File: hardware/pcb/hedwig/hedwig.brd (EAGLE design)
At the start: 60 x 60 mm, 85 parts, among them J1 DX07B024JJ1R1500, P1 JTAG-10MINI, P2 SENSOR_SCL, P3 RF_SCK, P4 PC1, P5 PC5, P6 PC9, Q1 16MHz, Q2 IRLML6402, Q3 20V/0.2A/8MHz/1.2Ω/1Vth, Q6 20V/0.2A/8MHz/1.2Ω/1Vth, U1 NRF24L01SMD, U2 TEXAS_INSTRUMENTS_TLC59731DRT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, U3 FT232RQ, U4 TPS7A26-1.8, U5 ADP2302, U6 9DoF IMU, U7 MPL3115A2LGA, X1 8M, X2 32.768

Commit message: Added pics, pdf, fixed silkscreen, and added more vias
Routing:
- net GND: vias 67 -> 99
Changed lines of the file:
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@@
 <layer number="25" name="tNames" color="7" fill="1" visible="yes" active="yes"/>
 <layer number="26" name="bNames" color="7" fill="1" visible="yes" active="yes"/>
-<layer number="27" name="tValues" color="7" fill="1" visible="no" active="yes"/>
-<layer number="28" name="bValues" color="7" fill="1" visible="no" active="yes"/>
+<layer number="27" name="tValues" color="7" fill="1" visible="yes" active="yes"/>
+<layer number="28" name="bValues" color="7" fill="1" visible="yes" active="yes"/>
 <layer number="29" name="tStop" color="7" fill="3" visible="yes" active="yes"/>
 <layer number="30" name="bStop" color="7" fill="6" visible="yes" active="yes"/>
@@
 <layer number="39" name="tKeepout" color="4" fill="11" visible="yes" active="yes"/>
 <layer number="40" name="bKeepout" color="1" fill="11" visible="yes" active="yes"/>
-<layer number="41" name="tRestrict" color="4" fill="10" visible="yes" active="yes"/>
-<layer number="42" name="bRestrict" color="1" fill="10" visible="yes" active="yes"/>
-<layer number="43" name="vRestrict" color="2" fill="10" visible="yes" active="yes"/>
-<layer number="44" name="Drills" color="7" fill="1" visible="yes" active="yes"/>
-<layer number="45" name="Holes" color="7" fill="1" visible="yes" active="yes"/>
-<layer number="46" name="Milling" color="3" fill="1" visible="yes" active="yes"/>
-<layer number="47" name="Measures" color="7" fill="1" visible="yes" active="yes"/>
-<layer number="48" name="Document" color="7" fill="1" visible="yes" active="yes"/>
-<layer number="49" name="Reference" color="7" fill="1" visible="yes" active="yes"/>
+<layer number="41" name="tRestrict" color="4" fill="10" visible="no" active="yes"/>
+<layer number="42" name="bRestrict" color="1" fill="10" visible="no" active="yes"/>
+<layer number="43" name="vRestrict" color="2" fill="10" visible="no" active="yes"/>
+<layer number="44" name="Drills" color="7" fill="1" visible="no" active="yes"/>
+<layer number="45" name="Holes" color="7" fill="1" visible="no" active="yes"/>
+<layer number="46" name="Milling" color="3" fill="1" visible="no" active="yes"/>
+<layer number="47" name="Measures" color="7" fill="1" visible="no" active="yes"/>
+<layer number="48" name="Document" color="7" fill="1" visible="no" active="yes"/>
+<layer number="49" name="Reference" color="7" fill="1" visible="no" active="yes"/>
 <layer number="50" name="dxf" color="7" fill="1" visible="no" active="no"/>
-<layer number="51" name="tDocu" color="7" fill="1" visible="yes" active="yes"/>
-<layer number="52" name="bDocu" color="7" fill="1" visible="yes" active="yes"/>
+<layer number="51" name="tDocu" color="7" fill="1" visible="no" active="yes"/>
+<layer number="52" name="bDocu" color="7" fill="1" visible="no" active="yes"/>
 <layer number="53" name="tGND_GNDA" color="7" fill="9" visible="no" active="no"/>
 <layer number="54" name="bGND_GNDA" color="1" fill="9" visible="no" active="no"/>
@@
 <layer number="99" name="SpiceOrder" color="7" fill="1" visible="no" active="no"/>
 <layer number="100" name="Muster" color="7" fill="1" visible="no" active="no"/>
-<layer number="101" name="Patch_Top" color="12" fill="4" visible="yes" active="yes"/>
+<layer number="101" name="Patch_Top" color="12" fill="4" visible="no" active="yes"/>
 <layer number="102" name="Vscore" color="7" fill="1" visible="no" active="yes"/>
 <layer number="103" name="tMap" color="7" fill="1" visible="no" active="yes"/>
@@
 <layer number="131" name="tAdjust" color="7" fill="1" visible="no" active="no"/>
 <layer number="132" name="bAdjust" color="7" fill="1" visible="no" active="no"/>
-<layer number="144" name="Drill_legend" color="7" fill="1" visible="yes" active="yes"/>
+<layer number="144" name="Drill_legend" color="7" fill="1" visible="no" active="yes"/>
 <layer number="150" name="Notes" color="7" fill="1" visible="no" active="no"/>
 <layer number="151" name="HeatSink" color="7" fill="1" visible="no" active="yes"/>
@@
 <layer number="155" name="FabDoc3" color="7" fill="1" visible="no" active="no"/>
 <layer number="199" name="Contour" color="7" fill="1" visible="no" active="no"/>
-<layer number="200" name="200bmp" color="1" fill="10" visible="yes" active="yes"/>
+<layer number="200" name="200bmp" color="1" fill="10" visible="no" active="yes"/>
 <layer number="201" name="201bmp" color="2" fill="10" visible="no" active="yes"/>
 <layer number="202" name="202bmp" color="3" fill="1" visible="no" active="no"/>
@@
 <text x="5.156140625" y="4.1582" size="0.3048" layer="22" rot="MR0">RF_MOSI</text>
 <text x="5.1028" y="0.1983375" size="0.3048" layer="22" rot="MR0">PC1</text>
-<text x="-137.5003625" y="10.09776875" size="0.3048" layer="22" rot="MR270">PC3</text>
+<text x="5.27176875" y="-3.8506375" size="0.3048" layer="22" rot="MR0">PC3</text>
 <text x="5.30091875" y="-7.8839375" size="0.3048" layer="22" rot="MR0">PC5</text>
 <text x="5.2425" y="-11.87046875" size="0.3048" layer="22" rot="MR0">PC7</text>
@@
 <rectangle x1="-16.8148" y1="1.27" x2="-16.7132" y2="1.3716" layer="22" rot="R90"/>
 <rectangle x1="-16.9164" y1="1.27" x2="-16.8148" y2="1.3716" layer="22" rot="R90"/>
-<text x="28.0416" y="-3.556" size="0.381" layer="22" font="vector" rot="R90">Designed by Adam in California
+<text x="27.9146" y="4.445" size="0.381" layer="22" font="vector" rot="MR270">Designed by Adam in California
       (while Devin watched)</text>
 </plain>
@@
 <via x="11.43" y="27.94" extent="1-16" drill="0.35"/>
 <via x="20.32" y="21.59" extent="1-16" drill="0.35"/>
+<via x="21.59" y="-3.81" extent="1-16" drill="0.35"/>
+<via x="26.67" y="17.78" extent="1-16" drill="0.35"/>
+<via x="24.13" y="17.78" extent="1-16" drill="0.35"/>
+<via x="19.05" y="19.05" extent="1-16" drill="0.35"/>
+<via x="20.32" y="15.24" extent="1-16" drill="0.35"/>
+<via x="26.67" y="13.97" extent="1-16" drill="0.35"/>
+<via x="25.4" y="8.89" extent="1-16" drill="0.35"/>
+<via x="13.97" y="20.32" extent="1-16" drill="0.35"/>
+<via x="25.4" y="15.24" extent="1-16" drill="0.35"/>
+<via x="25.4" y="19.05" extent="1-16" drill="0.35"/>
+<via x="12.7" y="-2.54" extent="1-16" drill="0.35"/>
+<via x="2.54" y="-12.7" extent="1-16" drill="0.35"/>
+<via x="-6.35" y="-26.67" extent="1-16" drill="0.35"/>
+<via x="2.54" y="-25.4" extent="1-16" drill="0.35"/>
+<via x="15.494" y="-10.16" extent="1-16" drill="0.35"/>
+<via x="26.416" y="-12.7" extent="1-16" drill="0.35"/>
+<via x="16.129" y="-4.191" extent="1-16" drill="0.35"/>
+<via x="25.527" y="-3.048" extent="1-16" drill="0.35"/>
+<via x="12.573" y="-13.081" extent="1-16" drill="0.35"/>
+<via x="20.574" y="-12.954" extent="1-16" drill="0.35"/>
+<via x="18.923" y="-22.352" extent="1-16" drill="0.35"/>
+<via x="9.779" y="-20.066" extent="1-16" drill="0.35"/>
+<via x="5.461" y="-17.018" extent="1-16" drill="0.35"/>
+<via x="6.731" y="-9.779" extent="1-16" drill="0.35"/>
+<via x="4.064" y="6.477" extent="1-16" drill="0.35"/>
+<via x="2.286" y="5.334" extent="1-16" drill="0.35"/>
+<via x="26.162" y="2.921" extent="1-16" drill="0.35"/>
+<via x="20.32" y="2.921" extent="1-16" drill="0.35"/>
+<via x="-22.86" y="-5.715" extent="1-16" drill="0.35"/>
+<via x="-19.05" y="-6.477" extent="1-16" drill="0.35"/>
+<via x="-26.289" y="-4.064" extent="1-16" drill="0.35"/>
+<via x="-25.781" y="-15.113" extent="1-16" drill="0.35"/>
 </signal>
 <signal name="NRST">

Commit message: Fix major issues in hardware
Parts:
- C10, C11, C8, C9: value 0.1uF -> 8.2pF
- C14: value 0.1uF -> 2.2uF
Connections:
- removed net B_VBUS: J1.B4, J1.B9
- removed net N$25: 5V_BAT.1, Q2.P3
- new net N$34: 5V_BAT.1, Q2.P2
- net +3V3: now also U$1.13
- net +5V: no longer Q2.P2
- net GND: now also U$1.12
- net USB_VCC: now also J1.B4, J1.B9
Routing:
- net N$25: track 35.3 -> 0.00 mm
- net +3V3: track 408.2 -> 416.8 mm
- net B_VBUS: track 6.42 -> 0.00 mm, vias 2 -> 0
- net +5V: track 30.5 -> 27.4 mm
- net USB_VCC: track 41.5 -> 42.5 mm

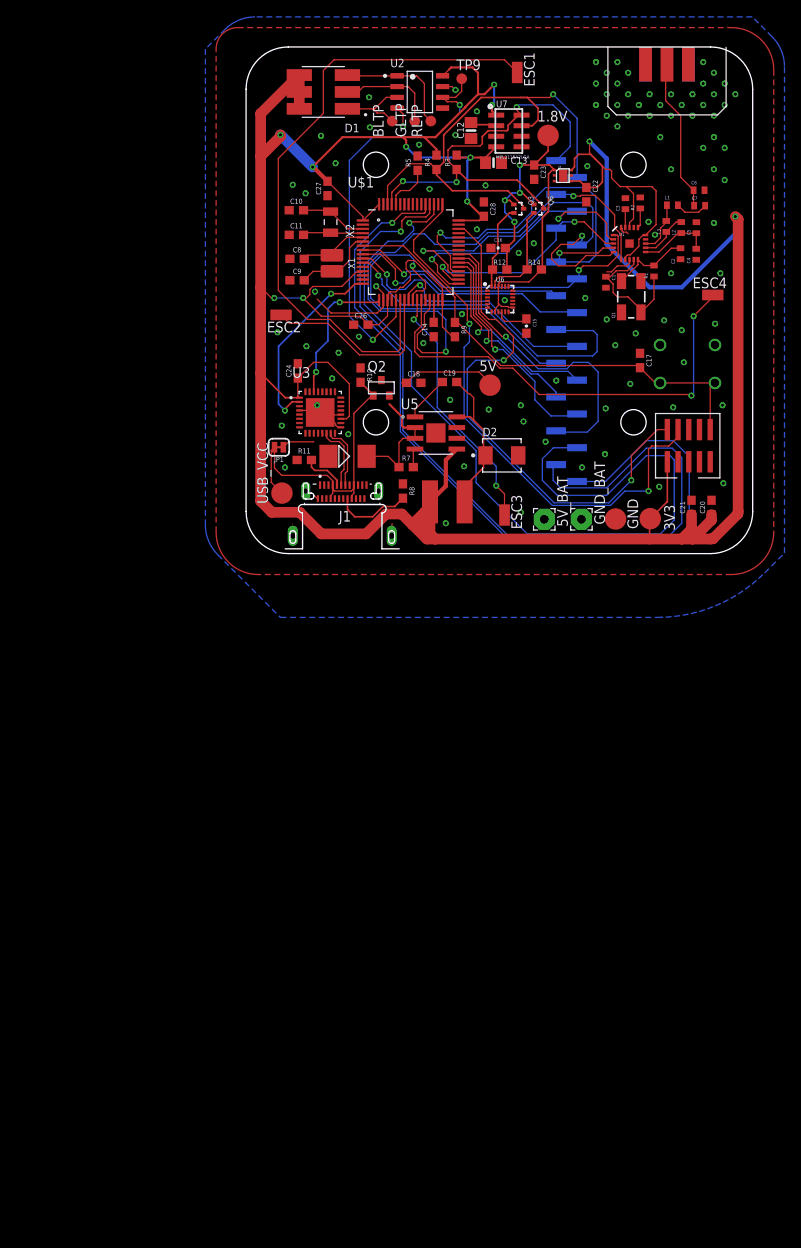
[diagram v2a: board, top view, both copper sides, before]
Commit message: schematic and pcb update
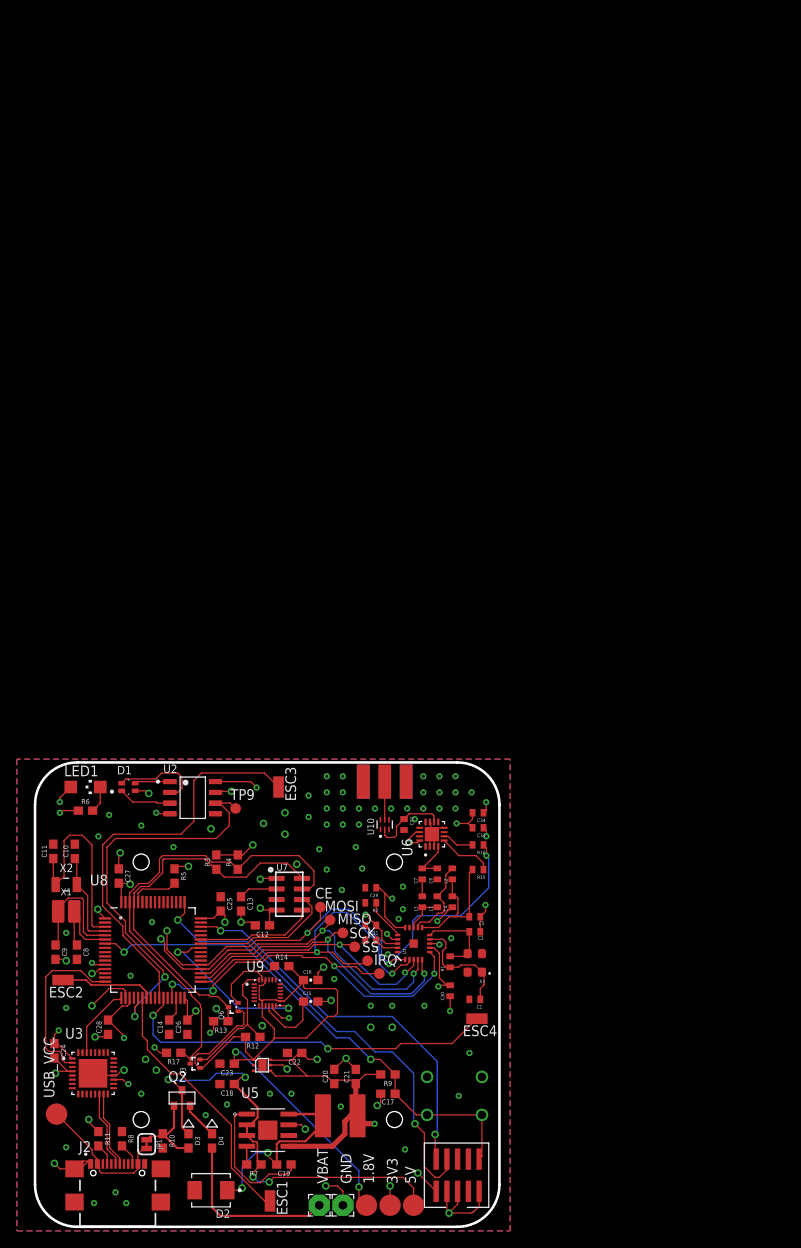
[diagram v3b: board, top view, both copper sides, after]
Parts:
- removed 5V_BAT, GND_BAT: (no value), wirepad:2,54/1,0
- removed BLTP, GLTP, RLTP: TPB1,27, testpad:B1,27
- removed J$1: SMA_EDGE, SparkFun:SMA-EDGE
- removed P2: SENSOR_SCL, falcon:STAGGERED-CONNECTOR
- removed P3: RF_SCK, falcon:STAGGERED-CONNECTOR
- removed P4: PC1, falcon:STAGGERED-CONNECTOR
- removed P5: PC5, falcon:STAGGERED-CONNECTOR
- removed P6: PC9, falcon:STAGGERED-CONNECTOR
- removed Q1: 16MHz, SparkFun:CRYSTAL-SMD-5X3
- removed U$1: STM32F412RE-S, mystm2:QFP50P1200X1200X160-64N
- removed U$2: PUSHBUTTON, falcon:PUSH_BUTTON
- removed U$4: 3uH, falcon:REG_INDUCTOR
- added C25: 0.1uF, SparkFun-Capacitors:0603
- added C29: 10nF, SparkFun:C0402
- added C30, C34: 0.1uF, SparkFun:C0402
- added C31: 1nF, SparkFun:C0402
- added C32: 0.3pF, SparkFun:C0402
- added C33: 220pF, SparkFun:C0402
- added CE, IRQ, MISO, MOSI, SCK, SS: TPB1,27, testpad:B1,27
- added D4: DIODE_0603, falcon:DIODE_0603
- added J2: USB4110-GF-A, USB4110-GF-A:GCT_USB4110-GF-A
- added J3: SMA_EDGE, SparkFun:SMA-EDGE
- added L4: 3uH, falcon:REG_INDUCTOR
- added LED1: (no value), led:CHIPLED_1206
- added R13, R17, R6: 10k, SparkFun-Resistors:0603
- added R15, R16: 10k, SparkFun:C0402
- added U10: 2450LP14A100T, 2450LP14A100T:ICCAF50P160X80X70-6N
- added U8: STM32F412RE-S, mystm2:QFP50P1200X1200X160-64N
- added U9: ICM-20948, ICM-20948:QFN40P300X300X105-24N
- added VBAT: (no value), wirepad:2,54/1,0
- added X3: ABM8-16.000MHZ-B2-T, ABM8-16.000MHZ-B2-T:OSCSC320X250X100N
- C10, C11, C8, C9: device SparkFun-Capacitors:0603 -> falcon:0603
- C12, C13: value 0.1µF -> 0.1uF; device microbuilder:0805-NO -> falcon:0603
- C18, C24: device SparkFun-Capacitors:0603@1 -> SparkFun-Capacitors:0603
- C19: value 0.1uF -> 0.22uF; device SparkFun-Capacitors:0603@1 -> SparkFun-Capacitors:0603
- C20, C21: value 47uF -> 0.22uF; device SparkFun-Capacitors:0603@1 -> SparkFun-Capacitors:0603
- C22, C23: value 47uF -> 4.7uF; device SparkFun-Capacitors:0603@1 -> SparkFun-Capacitors:0603
- D1: value SFT722N-S -> EVERLIGHT_EAST1616RGBB2EVERLIGHT_EAST1616RGBB2_0_0; device SFT722N-S:LED_SFT722N-S -> Everlight - EAST1616RGBB2:EVERLIGHT_EAST1616RGBB2_0
- D3: value SURS8360BT3G -> DIODE_0603; device falcon:SMB -> falcon:DIODE_0603
- GND: value TPB2,54 -> (none); device testpad:B2,54 -> wirepad:2,54/1,0
- J1: value DX07B024JJ1R1500 -> PUSHBUTTON; device DX07B024JJ1R1500:JAE_DX07B024JJ1R1500 -> falcon:PUSH_BUTTON
- L1: value 3.9nH -> 8.2nH
- L3: value 8.2nH -> 3.9nH
- R10, R12, R14: value 2.49k -> 10k
- R9: value 100k -> 10k
- U6: value 9DoF IMU -> RFX2401C; device SparkFun-Sensors:QFN24-3X3 -> RFX2401C:QFN50P300X300X60-17N
- moved ESC1 136.8 mm to (-27.2, -106.9)
- moved 1.8V 128.5 mm to (-15.7, -107.4), turned to 270 degrees
- moved C23 111.7 mm to (-32.3, -90.7), turned to 180 degrees
- moved U4 111.2 mm to (-28.1, -90.8)
- moved Q3 108.6 mm to (-36.6, -90.7), turned to 90 degrees
- moved C22 107.4 mm to (-24.3, -89.4), turned to 180 degrees
- moved C28 106.6 mm to (-46.4, -86.4), turned to 90 degrees
- moved Q6 101.6 mm to (-32.1, -84.0), turned to 90 degrees
- moved 5V 97.5 mm to (-10.2, -107.4)
- moved C12 97.3 mm to (-28.1, -74.3), turned to 180 degrees
- moved R12 95.5 mm to (-29.2, -87.5), turned to 180 degrees
- moved C19 94.7 mm to (-25.5, -102.6), turned to 180 degrees
- moved U7 94.1 mm to (-24.9, -70.6)
- moved R10 93.7 mm to (-39.9, -99.8), turned to 90 degrees
- moved D2 93.6 mm to (-34.2, -105.7), turned to 180 degrees
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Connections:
- removed net ADSD_STUB: U6.9
- removed net ANT: C6.2, C7.2, J$1.SIG
- removed net N$7: C4.1, C5.1, L2.1, U1.11
- removed net PC6: P5.2, U$1.37
- removed net REGOUT: C15.1, U6.10
- new net 5V_BAT: D4.A, VBAT.1
- new net ALT_IRQ_1: U7.P$6, U8.42
- new net ALT_IRQ_2: U7.P$5, U8.43
- new net IMU_IRQ: U8.41, U9.12
- new net N$25: LED1.C, R6.2
- new net N$37: C32.1, U10.2, U6.10
- new net N$39: C15.1, U9.10
- new net N$53: J3.SIG, U10.5
- new net N$57: R16.1, U6.6
- new net N$58: R15.1, U6.5
- new net PC0: U8.8
- new net TXRX: C6.2, C7.2, U6.4
- new net VDD_PA: C4.1, C5.1, L2.1, R15.2, U1.11
- net +3V3: now also C12.1, C25.2, C29.1, C30.1, C31.1, C33.2, C34.2, L4.@2, LED1.A, R13.2, R17.2, U6.14, U6.16, U8.1, U8.13, U8.19, U8.32, U8.48, U8.64; no longer C13.1, D1.5, D1.6, U$1.1, U$1.13, U$1.19, U$1.32, U$1.48, U$1.64, U$4.@2
- net +5V: now also D3.C, Q2.P3; no longer D3.@2
- net 1V8: now also U9.13, U9.22, U9.8; no longer U6.13, U6.22, U6.8
- net CAP: now also C13.1; no longer C12.1
- net GND: now also C10.2, C11.2, C25.1, C29.2, C30.2, C31.2, C32.2, C33.1, C34.1, C8.2, C9.2, GND.1, J1.3, J1.4, J2.A1/B12, J2.B1/A12, J2.S1, J2.S2, J2.S3, J2.S4, J3.GND@0, J3.GND@1, J3.GND@2, J3.GND@3, R6.1, U10.1, U10.3, U10.4, U10.6, U6.11, U6.17, U6.2, U6.3, U6.8, U6.9, U8.12, U8.18, U8.31, U8.47, U8.63, U9.11, U9.18, U9.20, U9.9, X3.2, X3.4; no longer C10.1, C11.1, C8.1, C9.1, GND.TP, GND_BAT.1, J$1.GND@0, J$1.GND@1, J$1.GND@2, J$1.GND@3, J1.A1, J1.A12, J1.B1, J1.B12, J1.SH1, J1.SH2, J1.SH3, J1.SH4, J1.SH5, J1.SH6, J1.SH7, J1.SH8, U$1.12, U$1.18, U$1.31, U$1.47, U$1.63, U$2.3, U$2.4, U6.18, U6.20
- net LED_SDO: now also U8.21; no longer U$1.21
- net MOTOR1: now also U8.22; no longer U$1.22
- net MOTOR2: now also U8.23; no longer U$1.23
- net MOTOR3: now also U8.26; no longer U$1.26
- net MOTOR4: now also U8.27; no longer U$1.27
- net N$1: now also X3.1; no longer Q1.1
- net N$10: now also C8.1, U8.6; no longer C9.2, U$1.6
- net N$11: no longer BLTP.TP
- net N$12: no longer RLTP.TP
- net N$13: now also C11.1, U8.3; no longer C10.2, U$1.3
- net N$14: now also C10.1, U8.4; no longer C11.2, U$1.4
- net N$15: now also J2.B5; no longer J1.B5
- net N$16: now also U8.60; no longer U$1.60
- net N$17: now also U8.30; no longer U$1.30
- net N$2: now also X3.3; no longer Q1.3
- net N$21: now also J2.A6; no longer J1.A6
- net N$22: now also J2.A7; no longer J1.A7
- net N$24: now also L4.@1; no longer U$4.@1
- net N$26: now also J2.A5; no longer J1.A5
- net N$27: no longer GLTP.TP
- net N$3: now also L1.1; no longer L3.1
- net N$34: now also D4.C; no longer 5V_BAT.1
- net N$6: now also L1.2, L3.1; no longer L1.1, L3.2
- net N$8: now also C9.1, U8.5; no longer C8.2, U$1.5
- net N$9: now also L3.2; no longer L1.2
- net NRST: now also J1.1, J1.2, U8.7; no longer U$1.7, U$2.1, U$2.2
- net PC1: now also U8.9; no longer P4.1, U$1.9
- net PC10: now also U8.51; no longer P6.2, U$1.51
- net PC11: now also U8.52; no longer P6.3, U$1.52
- net PC12: now also U8.53; no longer P6.4, U$1.53
- net PC13: now also U8.2; no longer U$1.2
- net PC2: now also U8.10; no longer P4.2, U$1.10
- net PC3: now also U8.11; no longer P4.3, U$1.11
- net PC4: now also U8.24; no longer P4.4, U$1.24
- net PC5: now also U8.25; no longer P5.1, U$1.25
- net PC7: now also U8.38; no longer P5.3, U$1.38
- net PC8: now also U8.39; no longer P5.4, U$1.39
- net PC9: now also U8.40; no longer P6.1, U$1.40
- net RF_CE: now also CE.TP, R16.2, U8.37; no longer P3.4, U$1.8
- net RF_IRQ: now also IRQ.TP, U8.29; no longer P2.3, U$1.29
- net RF_MISO: now also MISO.TP, U8.35; no longer P3.2, U$1.35
- net RF_MOSI: now also MOSI.TP, U8.36; no longer P3.3, U$1.36
- net RF_SCK: now also SCK.TP, U8.34; no longer P3.1, U$1.34
- net RF_SS: now also SS.TP, U8.33; no longer P2.4, U$1.33
- net SENSOR_SCL: now also R13.1, U8.61; no longer P2.1, U$1.61
- net SENSOR_SCL_LV: now also U9.23; no longer U6.23
- net SENSOR_SDA: now also R17.1, U8.62; no longer P2.2, U$1.62
- net SENSOR_SDA_LV: now also U9.24; no longer U6.24
- net SWCLK: now also U8.49; no longer U$1.49
- net SWDIO: now also U8.46; no longer U$1.46
- net USB_RX: now also U8.17; no longer U$1.17
- net USB_TX: now also U8.16; no longer U$1.16
- net USB_VCC: now also D3.A, J2.A4/B9, J2.B4/A9; no longer D3.@1, J1.A4, J1.A9, J1.B4, J1.B9
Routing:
- net +3V3: track 416.8 -> 127.7 mm, vias 11 -> 25
- net PC10: track 103.9 -> 0.00 mm, vias 1 -> 0
- net PC11: track 102.2 -> 0.00 mm, vias 1 -> 0
- net PC12: track 99.8 -> 0.00 mm, vias 1 -> 0
- net GND: track 29.9 -> 90.4 mm, vias 99 -> 102
- net MOTOR1: track 75.7 -> 31.3 mm
- net PC5: track 41.4 -> 0.00 mm, vias 1 -> 0
- net PC3: track 40.2 -> 0.00 mm, vias 1 -> 0
- net PC9: track 37.8 -> 0.00 mm, vias 1 -> 0
- net 1V8: track 51.3 -> 86.9 mm, vias 4 -> 2
- net PC2: track 29.7 -> 0.00 mm, vias 1 -> 0
- net PC8: track 29.6 -> 0.00 mm, vias 1 -> 0
- net +5V: track 27.4 -> 55.4 mm, vias 0 -> 4
- net PC1: track 26.7 -> 0.00 mm, vias 1 -> 0
- net RF_CE: track 37.5 -> 63.8 mm, vias 2 -> 4
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- added copper zone on layer 15, net +3V3
- added copper zone on layer 2, net GND
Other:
- board size 60 x 60 mm -> 55 x 55 mm
- board text removed: "PC1"
- board text removed: "PC10"
- board text removed: "PC11"
- board text removed: "PC12"
- board text removed: "PC2"
- board text removed: "PC3"
- board text removed: "PC4"
- board text removed: "PC5"
- board text removed: "PC6"
- board text removed: "PC7"
- board text removed: "PC8"
- board text removed: "PC9"
- board text removed: "RF_CE"
- board text removed: "RF_IRQ"
- board text removed: "RF_MISO"
- board text removed: "RF_MOSI"
- board text removed: "RF_SCK"
- board text removed: "RF_SS"
- board text removed: "SENSOR_SCL"
- board text removed: "SENSOR_SDA"

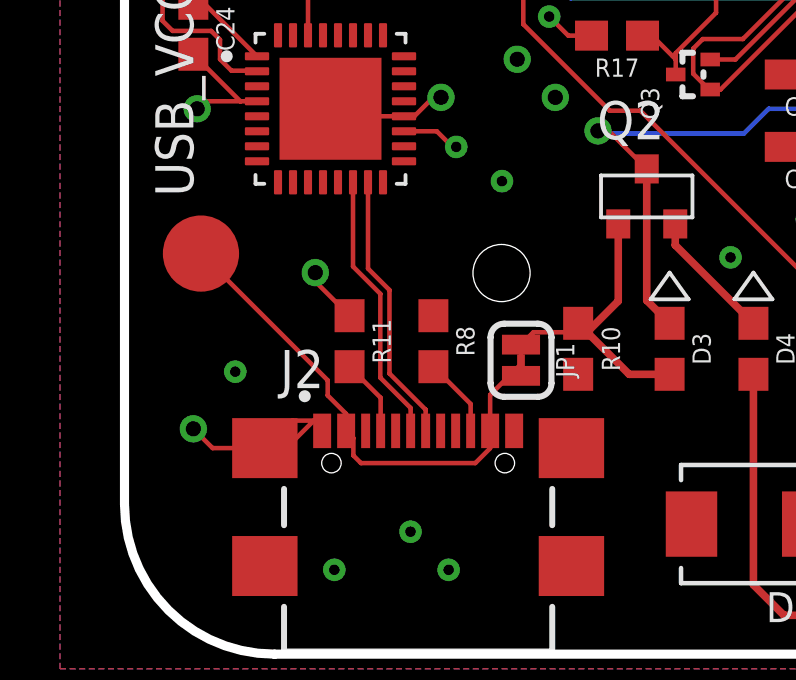
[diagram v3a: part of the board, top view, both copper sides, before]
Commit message: Schematic Update  - Fix USB C port reversablilty issue Board Update  - Fix USB C port reversablilty issue BOM Update  - Fix incorrect logic level shift FET  - Fix multiple entries for same parts
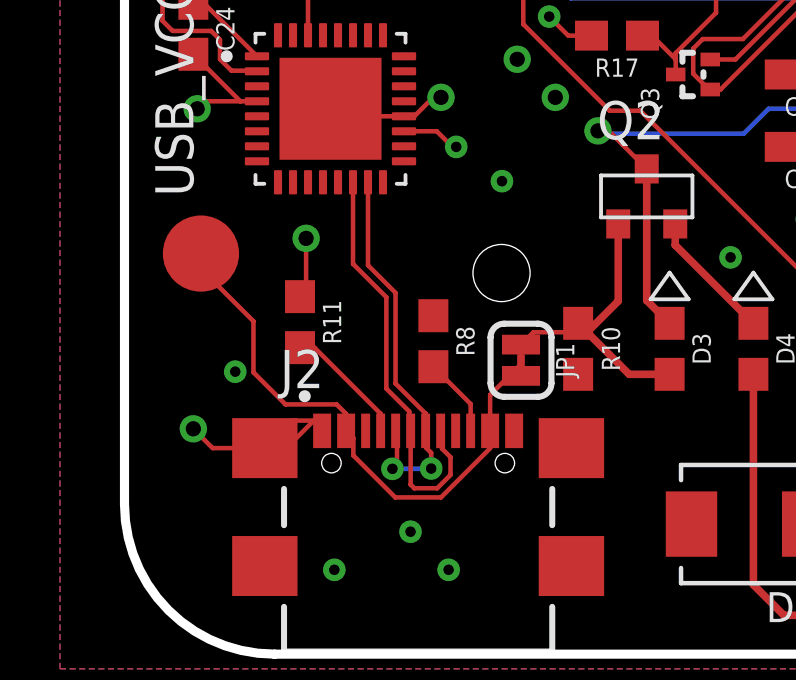
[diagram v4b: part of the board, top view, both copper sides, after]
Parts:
- moved R11 1.77 mm to (-49.1, -98.9)
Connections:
- removed net N$21: J2.A6, U3.14
- removed net N$22: J2.A7, U3.15
- new net USB_DN: J2.A7, J2.B7, U3.15
- new net USB_DP: J2.A6, J2.B6, U3.14
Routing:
- net USB_DP: track 0.00 -> 14.0 mm
- net USB_DN: track 0.00 -> 13.1 mm, vias 0 -> 2
- net N$22: track 9.08 -> 0.00 mm
- net N$21: track 9.08 -> 0.00 mm
- net N$26: track 2.57 -> 4.64 mm
- net USB_VCC: track 28.1 -> 30.1 mm
